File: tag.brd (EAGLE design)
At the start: 20.9 x 13.2 mm, 9 parts, among them X1 OMAT_IC_PIIKKIRIMA-8A, X2 OMAT_IC_PIIKKIRIMA-8B

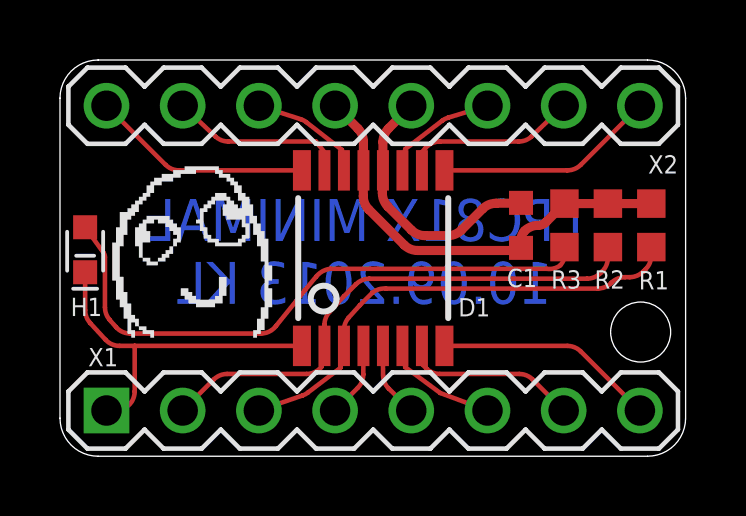
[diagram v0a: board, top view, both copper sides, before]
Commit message: VCC/GND Fixed
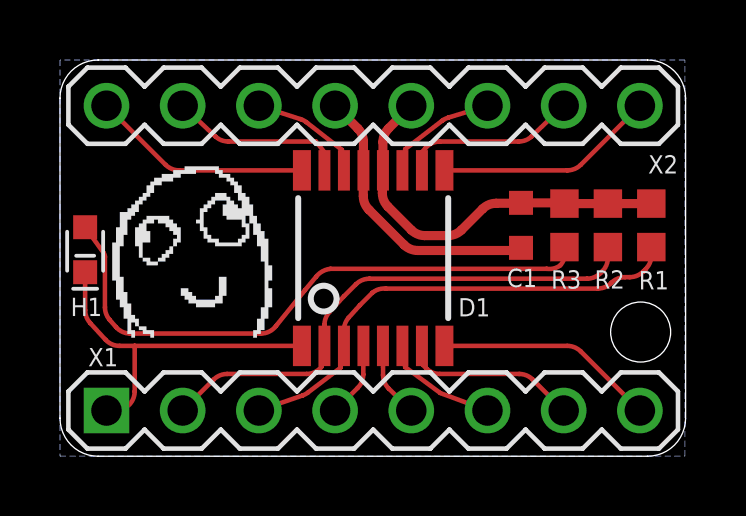
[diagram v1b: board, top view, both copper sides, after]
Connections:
- removed net N$15: C1.2, D1.12, X2.4
- removed net N$17: C1.1, D1.13, R1.2, R2.2, R3.2, X2.5
- new net +3V3: C1.2, D1.12, R1.2, R2.2, R3.2, X2.4
- new net GND: C1.1, D1.13, X2.5
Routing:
- net N$17: track 14.6 -> 0.00 mm
- net +3V3: track 0.00 -> 13.3 mm
- net GND: track 0.00 -> 9.49 mm
- net N$15: track 8.93 -> 0.00 mm
- added copper zone on layer 16, net GND
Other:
- board text added: "LPC81X MINIMAL 27.09.2013 KL"
- board text removed: "LPC81X MINIMAL 10.09.2013 KL"
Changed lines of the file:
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@@
 <setting verticaltext="up"/>
 </settings>
-<grid distance="0.001" unitdist="inch" unit="inch" style="lines" multiple="1" display="no" altdistance="0.025" altunitdist="inch" altunit="inch"/>
+<grid distance="0.01" unitdist="inch" unit="inch" style="lines" multiple="1" display="no" altdistance="0.025" altunitdist="inch" altunit="inch"/>
 <layers>
 <layer number="1" name="Top" color="4" fill="1" visible="yes" active="yes"/>
@@
 <layer number="27" name="tValues" color="7" fill="1" visible="yes" active="yes"/>
 <layer number="28" name="bValues" color="7" fill="1" visible="yes" active="yes"/>
-<layer number="29" name="tStop" color="7" fill="3" visible="no" active="yes"/>
-<layer number="30" name="bStop" color="7" fill="6" visible="no" active="yes"/>
+<layer number="29" name="tStop" color="7" fill="3" visible="yes" active="yes"/>
+<layer number="30" name="bStop" color="7" fill="6" visible="yes" active="yes"/>
 <layer number="31" name="tCream" color="7" fill="4" visible="yes" active="yes"/>
 <layer number="32" name="bCream" color="7" fill="5" visible="yes" active="yes"/>
@@
 <wire x1="0" y1="1.27" x2="1.27" y2="0" width="0" layer="20" curve="90"/>
 <hole x="19.3548" y="4.1402" drill="2"/>
-<text x="10.16" y="5.08" size="1.397" layer="16" font="vector" ratio="12" rot="MR0" align="bottom-center">LPC81X MINIMAL
-10.09.2013 KL</text>
 <text x="10.16" y="5.08" size="1.397" layer="30" font="vector" ratio="12" rot="MR0" align="bottom-center">LPC81X MINIMAL
-10.09.2013 KL</text>
+27.09.2013 KL</text>
 </plain>
 <attributes>
@@
 <wire x1="12.937871875" y1="11.28585625" x2="14.2494" y2="11.684" width="0.1524" layer="1"/>
 </signal>
-<signal name="N$15">
+<signal name="+3V3">
+<contactref element="R2" pad="2"/>
+<contactref element="R3" pad="2"/>
+<contactref element="R1" pad="2"/>
+<wire x1="16.8148" y1="8.4212" x2="18.2626" y2="8.4212" width="0.3048" layer="1"/>
+<wire x1="19.7104" y1="8.4212" x2="18.2626" y2="8.4212" width="0.3048" layer="1"/>
 <contactref element="X2" pad="4"/>
 <contactref element="C1" pad="2"/>
@@
 <wire x1="14.537825" y1="8.4328" x2="15.3536" y2="8.4328" width="0.3048" layer="1"/>
 <wire x1="15.3536" y1="8.4328" x2="15.367" y2="8.4462" width="0.3048" layer="1"/>
-</signal>
-<signal name="N$17">
+<wire x1="15.367" y1="8.4462" x2="16.8148" y2="8.4462" width="0.3048" layer="1"/>
+<wire x1="16.8148" y1="8.4462" x2="16.8148" y2="8.4212" width="0.3048" layer="1"/>
+</signal>
+<signal name="N$18">
+<contactref element="X2" pad="6"/>
+<contactref element="D1" pad="14"/>
+<wire x1="9.4644" y1="9.529" x2="9.398" y2="10.2108" width="0.1524" layer="1"/>
+<wire x1="9.398" y1="10.2108" x2="8.21675625" y2="11.13216875" width="0.1524" layer="1"/>
+<wire x1="8.21675625" y1="11.13216875" x2="8.02085625" y2="11.235903125" width="0.1524" layer="1" curve="20.104235"/>
+<wire x1="8.02085625" y1="11.235903125" x2="6.6294" y2="11.684" width="0.1524" layer="1"/>
+</signal>
+<signal name="N$19">
+<contactref element="X2" pad="7"/>
+<contactref element="D1" pad="15"/>
+<wire x1="8.8144" y1="9.529" x2="8.8144" y2="10.134" width="0.1524" layer="1"/>
+<wire x1="8.8144" y1="10.134" x2="8.5344" y2="10.4902" width="0.1524" layer="1"/>
+<wire x1="8.5344" y1="10.4902" x2="5.610996875" y2="10.4902" width="0.1524" layer="1"/>
+<wire x1="5.610996875" y1="10.4902" x2="5.176078125" y2="10.662521875" width="0.1524" layer="1" curve="-43.228617"/>
+<wire x1="5.176078125" y1="10.662521875" x2="4.0894" y2="11.684" width="0.1524" layer="1"/>
+</signal>
+<signal name="N$20">
+<contactref element="D1" pad="16"/>
+<contactref element="X2" pad="8"/>
+<wire x1="8.0644" y1="9.529" x2="3.967425" y2="9.529" width="0.1524" layer="1"/>
+<wire x1="3.967425" y1="9.529" x2="3.5184125" y2="9.7149875" width="0.1524" layer="1" curve="-45"/>
+<wire x1="3.5184125" y1="9.7149875" x2="1.5494" y2="11.684" width="0.1524" layer="1"/>
+</signal>
+<signal name="GND">
 <contactref element="D1" pad="13"/>
 <contactref element="C1" pad="1"/>
 <contactref element="X2" pad="5"/>
-<contactref element="R2" pad="2"/>
-<contactref element="R3" pad="2"/>
-<contactref element="R1" pad="2"/>
 <wire x1="10.1144" y1="9.529" x2="10.1144" y2="10.475975" width="0.3048" layer="1"/>
 <wire x1="10.1144" y1="10.475975" x2="9.9284125" y2="10.9249875" width="0.3048" layer="1" curve="45"/>
@@
 <wire x1="10.1092" y1="8.670425" x2="10.1092" y2="9.5238" width="0.3048" layer="1"/>
 <wire x1="10.1092" y1="9.5238" x2="10.1144" y2="9.529" width="0.3048" layer="1"/>
-<wire x1="16.8148" y1="8.4212" x2="18.2626" y2="8.4212" width="0.3048" layer="1"/>
-<wire x1="19.7104" y1="8.4212" x2="18.2626" y2="8.4212" width="0.3048" layer="1"/>
 <wire x1="15.2788" y1="6.858" x2="15.367" y2="6.9462" width="0.3048" layer="1"/>
-<wire x1="15.367" y1="6.9462" x2="15.367" y2="7.223375" width="0.3048" layer="1"/>
-<wire x1="15.367" y1="7.223375" x2="15.4858125" y2="7.5102125" width="0.3048" layer="1" curve="-45"/>
-<wire x1="15.4858125" y1="7.5102125" x2="15.934825" y2="7.6962" width="0.3048" layer="1" curve="-45"/>
-<wire x1="15.934825" y1="7.6962" x2="16.199384375" y2="7.805784375" width="0.3048" layer="1" curve="45"/>
-<wire x1="16.199384375" y1="7.805784375" x2="16.8148" y2="8.4212" width="0.3048" layer="1"/>
-</signal>
-<signal name="N$18">
-<contactref element="X2" pad="6"/>
-<contactref element="D1" pad="14"/>
-<wire x1="9.4644" y1="9.529" x2="9.398" y2="10.2108" width="0.1524" layer="1"/>
-<wire x1="9.398" y1="10.2108" x2="8.21675625" y2="11.13216875" width="0.1524" layer="1"/>
-<wire x1="8.21675625" y1="11.13216875" x2="8.02085625" y2="11.235903125" width="0.1524" layer="1" curve="20.104235"/>
-<wire x1="8.02085625" y1="11.235903125" x2="6.6294" y2="11.684" width="0.1524" layer="1"/>
-</signal>
-<signal name="N$19">
-<contactref element="X2" pad="7"/>
-<contactref element="D1" pad="15"/>
-<wire x1="8.8144" y1="9.529" x2="8.8144" y2="10.134" width="0.1524" layer="1"/>
-<wire x1="8.8144" y1="10.134" x2="8.5344" y2="10.4902" width="0.1524" layer="1"/>
-<wire x1="8.5344" y1="10.4902" x2="5.610996875" y2="10.4902" width="0.1524" layer="1"/>
-<wire x1="5.610996875" y1="10.4902" x2="5.176078125" y2="10.662521875" width="0.1524" layer="1" curve="-43.228617"/>
-<wire x1="5.176078125" y1="10.662521875" x2="4.0894" y2="11.684" width="0.1524" layer="1"/>
-</signal>
-<signal name="N$20">
-<contactref element="D1" pad="16"/>
-<contactref element="X2" pad="8"/>
-<wire x1="8.0644" y1="9.529" x2="3.967425" y2="9.529" width="0.1524" layer="1"/>
-<wire x1="3.967425" y1="9.529" x2="3.5184125" y2="9.7149875" width="0.1524" layer="1" curve="-45"/>
-<wire x1="3.5184125" y1="9.7149875" x2="1.5494" y2="11.684" width="0.1524" layer="1"/>
+<polygon width="0.3048" layer="16">
+<vertex x="0" y="0"/>
+<vertex x="20.828" y="0"/>
+<vertex x="20.828" y="13.208"/>
+<vertex x="0" y="13.208"/>
+</polygon>
 </signal>
 </signals>
